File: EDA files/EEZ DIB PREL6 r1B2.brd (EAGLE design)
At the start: 146 x 95 mm, 66 parts, among them IC1 STM32F030C6T6, IC2 74HC1G126GW,125, IC3 M24C32-WMN6P, IC4 LP2985-33DBVR, K1 RT424005, K2 RT424005, K3 RT424005, K4 RT424005, K5 RT424005, K6 RT424005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

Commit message: #1 fixed
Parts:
- C2, C8, C9: device rcl:C1206 -> rcl:C0805
- moved C2 0.60 mm to (116.8, 20.8)
- moved C9 0.45 mm to (86.3, 16.8)
- moved C8 0.38 mm to (86.9, 20.7)
- moved C1 0.06 mm to (117.2, 22.6)
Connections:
- net +3V3: now also IC1.9; no longer IC1.8
- net GND: now also IC1.8; no longer IC1.9
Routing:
- net +3V3: track 85.6 -> 84.8 mm
- net GND: track 253.3 -> 252.8 mm
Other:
- board text added: "EEZ DIB PREL6 (04/2020 r1B2)"
- board text added: "EEZ DIB PREL6 (04/2020 r1B2) Project source code: github.com/eez-open"
- board text removed: "EEZ DIB PREL6 (03/2020 r1B1)"
- board text removed: "EEZ DIB PREL6 (03/2020 r1B1) Project source code: github.com/eez-open"

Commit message: #2
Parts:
- moved C3 1.78 mm to (135.1, 29.5)
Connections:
- net BOOT0: now also X2.26
- net GND: no longer X2.26
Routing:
- net BOOT0: track 24.7 -> 44.9 mm, vias 2 -> 3
- net +5V: track 360.4 -> 362.2 mm
- net GND: track 252.8 -> 254.0 mm

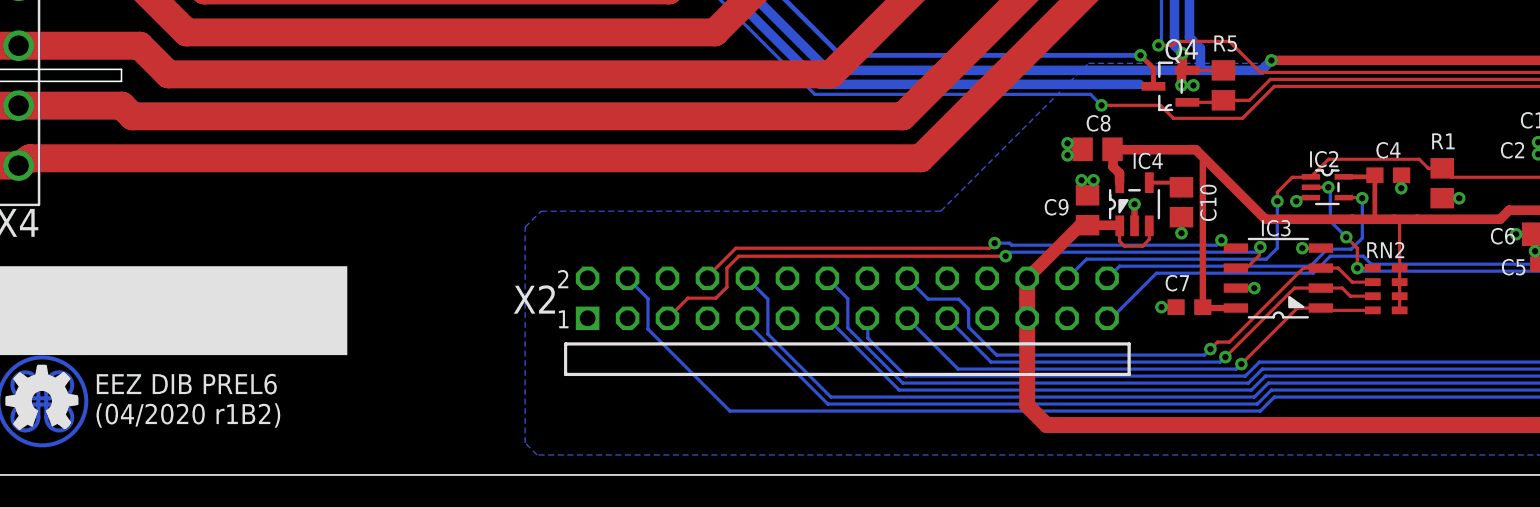
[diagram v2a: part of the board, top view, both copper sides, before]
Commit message: swap UART TX and RX
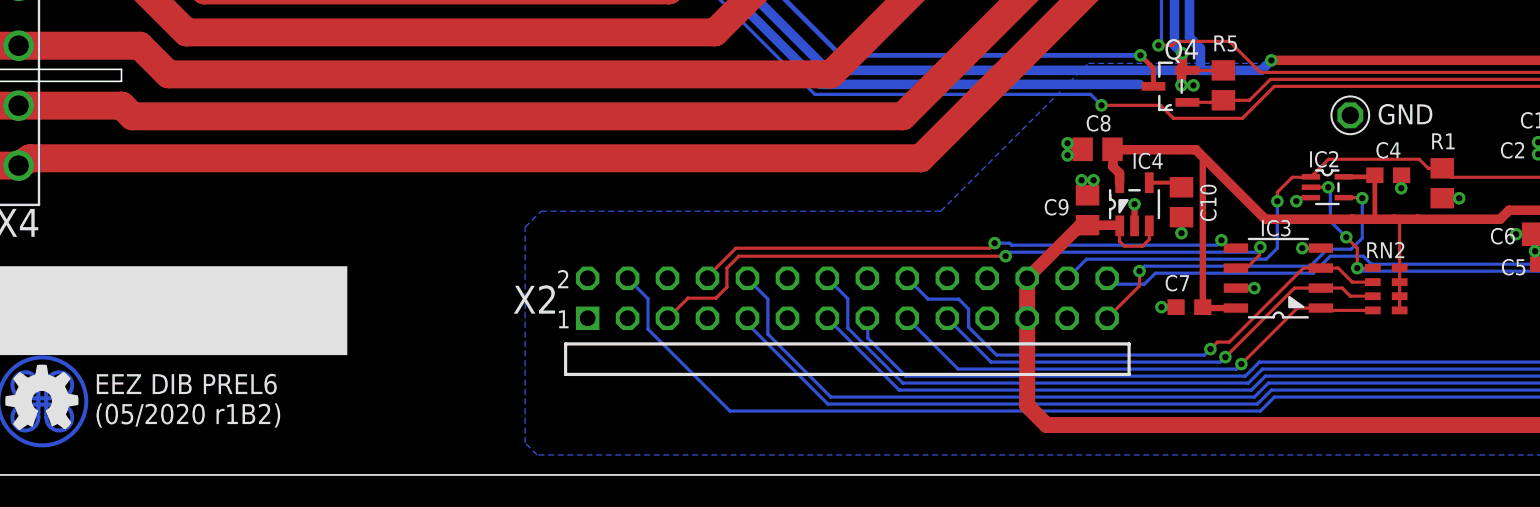
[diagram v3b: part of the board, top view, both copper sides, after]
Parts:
- added GND: (no value), EEZ_Lib1:PCB_SHIELD_TAB
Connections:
- removed net N$72: IC2.4, X2.28
- new net DIB_UART_RX: IC2.4, X2.27
- net GND: now also GND.1
- net UART_RX: now also X2.28; no longer X2.27
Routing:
- net DIB_UART_RX: track 0.00 -> 22.6 mm, vias 0 -> 2
- net N$72: track 21.0 -> 0.00 mm, vias 1 -> 0
- net UART_RX: track 43.3 -> 42.6 mm
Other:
- board text added: "EEZ DIB PREL6 (05/2020 r1B2)"
- board text added: "EEZ DIB PREL6 (05/2020 r1B2) Project source code: github.com/eez-open"
- board text removed: "EEZ DIB PREL6 (04/2020 r1B2)"
- board text removed: "EEZ DIB PREL6 (04/2020 r1B2) Project source code: github.com/eez-open"
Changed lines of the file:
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@@
 <dimension x1="-10" y1="81" x2="-11" y2="17" x3="-12" y3="49" textsize="2" layer="47" dtype="vertical"/>
 <text x="23.1675" y="3.2345" size="1.27" layer="21" font="vector" ratio="10" rot="SR0">EEZ DIB PREL6
-(04/2020 r1B2)</text>
-<text x="141.1565" y="48.9245" size="1.27" layer="22" font="vector" ratio="10" rot="SMR90">EEZ DIB PREL6 (04/2020 r1B2)
+(05/2020 r1B2)</text>
+<text x="141.1565" y="48.9245" size="1.27" layer="22" font="vector" ratio="10" rot="SMR90">EEZ DIB PREL6 (05/2020 r1B2)
 Project source code: github.com/eez-open</text>
 <rectangle x1="17.145" y1="7.62" x2="39.243" y2="13.2715" layer="21"/>
@@
 <attribute name="VALUE" x="133.2865" y="8.8265" size="1.016" layer="27" ratio="10" rot="R90"/>
 </element>
+<element name="GND" library="EEZ_Lib1" package="PCB_SHIELD_TAB" value="" x="102.997" y="22.86" smashed="yes">
+<attribute name="NAME" x="104.7115" y="22.2885" size="1.27" layer="25" ratio="10"/>
+</element>
 </elements>
 <signals>
@@
 <wire x1="134.366" y1="25.8445" x2="135.0645" y2="25.8445" width="0.3048" layer="1"/>
 <wire x1="135.0645" y1="25.8445" x2="135.0645" y2="27.1145" width="0.3048" layer="1"/>
+<contactref element="GND" pad="1"/>
 </signal>
 <signal name="DIB_A0">
@@
 </signal>
 <signal name="UART_RX">
-<contactref element="X2" pad="27"/>
 <via x="124.587" y="16.891" extent="1-16" drill="0.4" shape="octagon"/>
 <wire x1="101.727" y1="13.9065" x2="100.6475" y2="12.827" width="0.2032" layer="16"/>
@@
 <wire x1="124.587" y1="16.891" x2="125.095" y2="16.891" width="0.2032" layer="1"/>
 <wire x1="125.095" y1="16.891" x2="125.603" y2="16.383" width="0.2032" layer="1"/>
-<wire x1="87.54" y1="9.96" x2="87.811" y2="9.96" width="0.2032" layer="16"/>
-<wire x1="87.811" y1="9.96" x2="90.678" y2="12.827" width="0.2032" layer="16"/>
-<wire x1="90.678" y1="12.827" x2="100.6475" y2="12.827" width="0.2032" layer="16"/>
+<contactref element="X2" pad="28"/>
+<wire x1="100.6475" y1="12.827" x2="90.6145" y2="12.827" width="0.2032" layer="16"/>
+<wire x1="90.6145" y1="12.827" x2="89.916" y2="12.1285" width="0.2032" layer="16"/>
+<wire x1="89.916" y1="12.1285" x2="87.9115" y2="12.1285" width="0.2032" layer="16"/>
+<wire x1="87.9115" y1="12.1285" x2="87.54" y2="12.5" width="0.2032" layer="16"/>
 </signal>
 <signal name="SWCLK">
@@
 <wire x1="128.974" y1="6.419" x2="128.9685" y2="6.4135" width="0.2032" layer="1"/>
 </signal>
-<signal name="N$72">
-<contactref element="X2" pad="28"/>
+<signal name="DIB_UART_RX">
 <contactref element="IC2" pad="4"/>
 <via x="103.759" y="17.5895" extent="1-16" drill="0.4" shape="octagon"/>
@@
 <wire x1="102.5779" y1="17.6276" x2="103.7209" y2="17.6276" width="0.2032" layer="1"/>
 <wire x1="103.7209" y1="17.6276" x2="103.759" y2="17.5895" width="0.2032" layer="1"/>
-<wire x1="87.54" y1="12.5" x2="87.557" y2="12.5" width="0.2032" layer="16"/>
-<wire x1="87.557" y1="12.5" x2="88.3285" y2="13.2715" width="0.2032" layer="16"/>
-<wire x1="88.3285" y1="13.2715" x2="100.457" y2="13.2715" width="0.2032" layer="16"/>
+<contactref element="X2" pad="27"/>
+<wire x1="100.457" y1="13.2715" x2="89.916" y2="13.2715" width="0.2032" layer="16"/>
+<via x="89.5985" y="12.954" extent="1-16" drill="0.4" shape="octagon"/>
+<wire x1="89.5985" y1="12.954" x2="89.5985" y2="12.0185" width="0.2032" layer="1"/>
+<wire x1="89.5985" y1="12.0185" x2="87.54" y2="9.96" width="0.2032" layer="1"/>
+<wire x1="89.916" y1="13.2715" x2="89.5985" y2="12.954" width="0.2032" layer="16"/>
 </signal>
 <signal name="N$1">

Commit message: IRQ selection jumper
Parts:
- added DIB1.1: JP3-CUT-0805-ROTATED, EEZ_Lib1:JP3-0805-CUT2
- C5: value 100n -> 1u; device rcl:C0603 -> rcl:C0805
- C6: value 1u -> 100n; device rcl:C0805 -> rcl:C0603
- moved C5 1.93 mm to (115.5, 15.3), turned to 0 degrees
- moved C6 1.93 mm to (115.8, 13.4), turned to 180 degrees
- moved D3 0.51 mm to (134.9, 78.1)
- moved D6 0.51 mm to (134.9, 42.9)
- moved ZD3 0.51 mm to (134.9, 82.5)
- moved ZD6 0.51 mm to (134.9, 47.4)
- moved D2 0.25 mm to (99.1, 78.1)
- moved D5 0.25 mm to (99.1, 42.9)
- moved ZD2 0.25 mm to (99.1, 82.5)
- moved ZD5 0.25 mm to (99.1, 47.4)
- moved D1 0.25 mm to (63.5, 78.1)
- moved D4 0.25 mm to (63.5, 42.9)
- moved ZD1 0.25 mm to (63.5, 82.5)
- moved ZD4 0.25 mm to (63.5, 47.4)
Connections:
- new net DIB_CSB: DIB1.1.NO, X2.12
- new net N$13: DIB1.1.COM, IC1.33
- net +3V3: now also C5.2, C6.1; no longer C5.1, C6.2
- net DIB_IRQ: now also DIB1.1.NC; no longer IC1.33
- net GND: now also C5.1, C6.2; no longer C5.2, C6.1
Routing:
- net N$13: track 0.00 -> 94.3 mm, vias 0 -> 2
- net DIB_IRQ: track 85.2 -> 4.63 mm
- net DIB_CSB: track 0.00 -> 13.4 mm, vias 0 -> 1
- net +5V: track 362.2 -> 364.1 mm
- net N$69: track 69.5 -> 68.9 mm
- net N$7: track 8.63 -> 9.14 mm
- net N$100: track 8.63 -> 9.14 mm
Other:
- board text added: "EEZ DIB PREL6 (07/2020 r1B2)"
- board text added: "EEZ DIB PREL6 (07/2020 r1B2) Project source code: github.com/eez-open"
- board text removed: "EEZ DIB PREL6 (05/2020 r1B2)"
- board text removed: "EEZ DIB PREL6 (05/2020 r1B2) Project source code: github.com/eez-open"
